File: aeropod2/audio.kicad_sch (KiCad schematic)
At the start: 17 parts, among them J4 AudioJack3_Ground, U5 PCM5102A

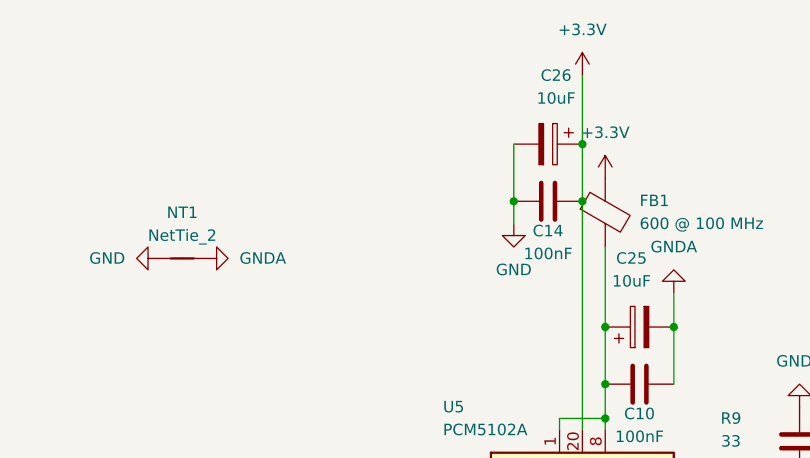
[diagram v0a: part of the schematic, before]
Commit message: Drop button pull-ups and backlight pin, clear ERC, vendor CP2102N footprint
The five button pull-ups are gone. The only line that actually needed one
was B5, because it sat on GPIO35 and GPIO34-39 are input only with no
internal pull-up. B5 now sits on GPIO33, a full GPIO, so the ESP32's own
pull-ups hold all five buttons high and R20-R24 are removed. GPIO35 is
spare.

The display connector goes back to seven pins. There is no backlight
control line, so the module's BL input is tied to 3.3 V and runs at full
brightness. The LEDC setup is removed and display_backlight() is a no-op
so callers do not change.

The five power_pin_not_driven errors are now properly resolved with
PWR_FLAGs on GND, VBUS, VSYS, AVDD and GNDA. To be clear about the VSS
one: that check looks for a power output pin on each rail and finds none
on a rail fed through a diode, ferrite or net tie. It was never a wiring
fault. Before the fixes it named J5 pin 3 CMD, because CMD was wrongly on
the GND net; afterwards it named J5 pin 6 VSS, which is the card's ground
pin and belongs there. The name moved because CMD left the ground net,
which is what the fix was for. Schematic is now 0 errors, 0 warnings.

The microSD wiring was re-verified pin by pin against the SD spec in SPI
mode: DAT2 and DAT1 unused, CS on DAT3/CD, MOSI on CMD, MISO on DAT0,
CLK on pin 5, VDD on pin 4, VSS on GND. All eight correct.

Footprints for every one of the 67 components were checked against what
is on disk. U6 was pointing at a vendor library in a Downloads folder
via a global nickname, so it built here and nowhere else. That library is
now vendored at aeropod2/footprints.pretty with a project fp-lib-table.

Also gitignores KiCad .lck session files.
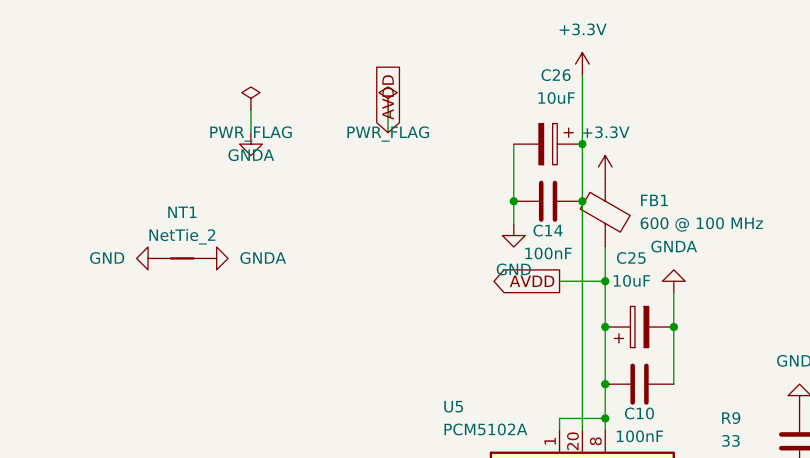
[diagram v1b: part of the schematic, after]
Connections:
- net AVDD: now reaches C10.1, C25.1, FB1.2, U5.1 (CPVDD), U5.8 (AVDD)

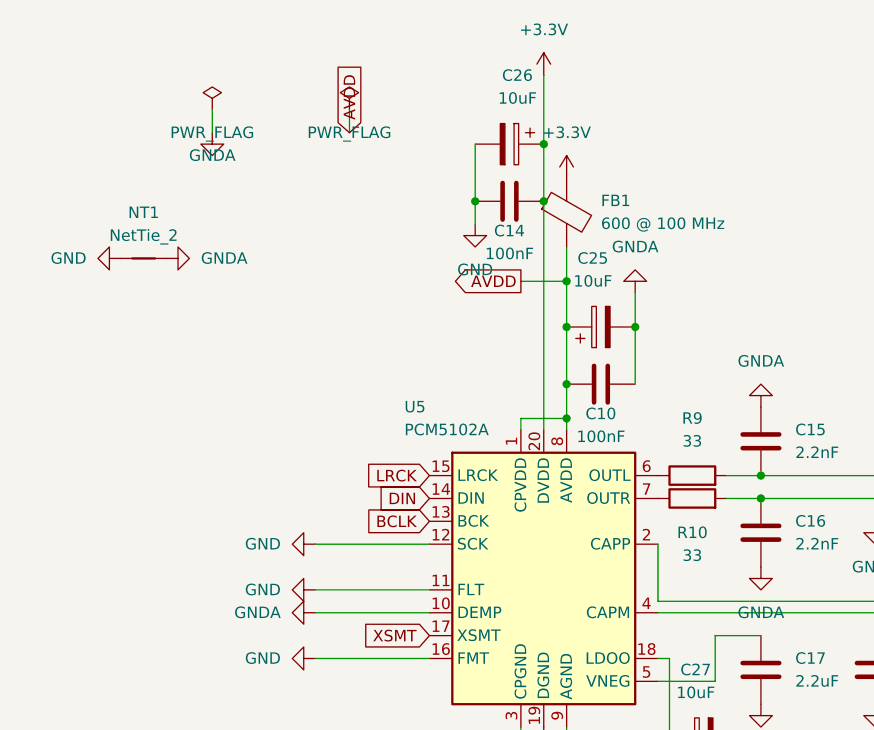
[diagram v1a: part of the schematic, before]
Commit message: Revert schematic, PCB and firmware to the hand-drawn version
Restores aeropod2/*.kicad_sch, aeropod2.kicad_pcb, the firmware pin map
and the BOM to their state at d6429d0, which is byte identical to the
last human-edited revision (2867710). The corrected schematic is still
in history at b35a9fa if any of it is wanted later.

The board file had picked up R18/R19 and the tactile switch footprints
from a schematic update. Nothing hand-made was lost reverting it: track
and via counts were unchanged at 894/147 and the two new parts were
sitting at KiCad's default drop position.

ELECTRICAL_REVIEW.md is rewritten to describe the faults as they stand
in this schematic, and to give the smallest set of layout changes that
makes the board work rather than the full correction.
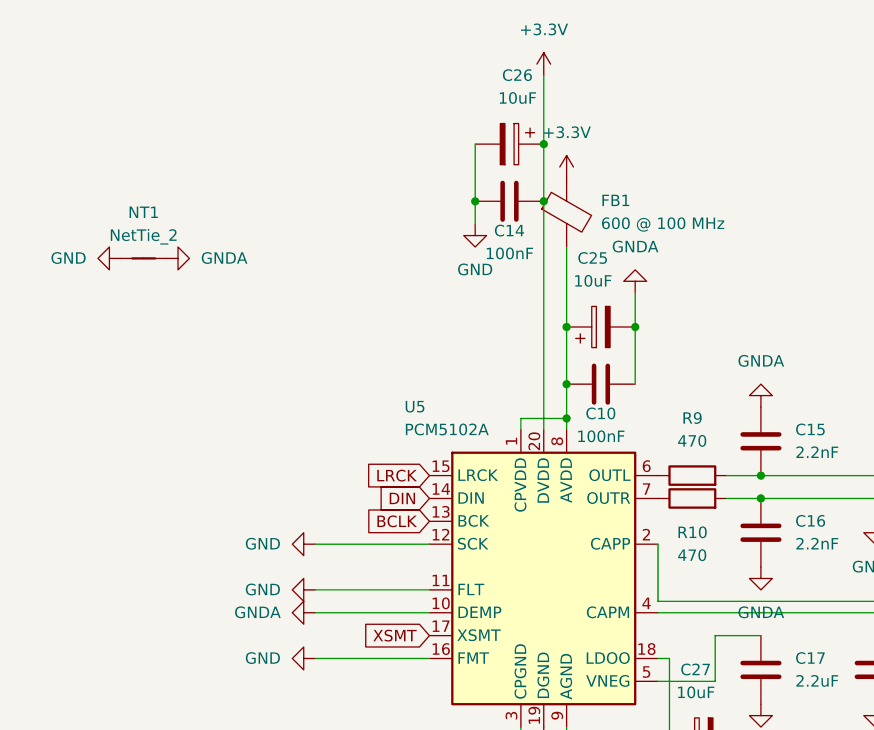
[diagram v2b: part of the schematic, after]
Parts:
- R10, R9: value 33 -> 470
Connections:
- net AVDD: no longer names the net of C10.1, C25.1, FB1.2, U5.1 (CPVDD), U5.8 (AVDD)

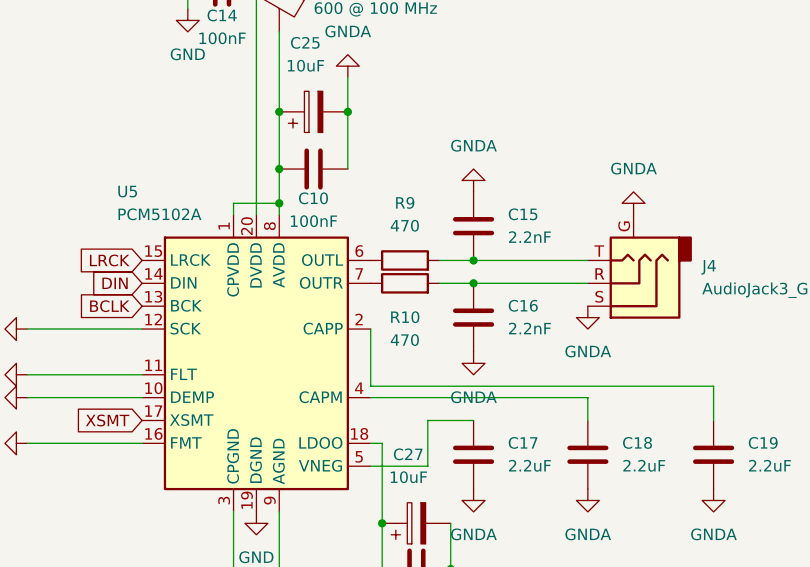
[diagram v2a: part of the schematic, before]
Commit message: Fix schematic faults found in electrical review, add reset/boot buttons
Four faults would have stopped the main board working:

- EN had no pull-up. R4/C5 sat on the unused throw of SW1 while EN was
  left holding only an AC coupled cap, so the module would not have
  booted. R4/C5 now sit on EN, and SW1/SW2 are momentary buttons to
  ground instead of slide switches.
- The microSD was miswired: connections shifted by one pin and CMD tied
  to GND, so no card could ever initialise. The display data line also
  shared a net with the card's DAT0 output. CS now lands on DAT3/CD,
  CMD on IO23 alongside the display, and IO19 is MISO from the card
  alone.
- The boost inductor was never connected to the input rail, so the
  MT3608 had nothing to pump. Rebuilt as VREGIN to L1 to SW plus diode
  anode, with the output caps and feedback divider past the diode.
- The 3.3 V rail had no headroom. R17 is now 100k, putting the boost
  near 5.1 V so the AMS1117 can actually regulate.

Also: backlight control on a new J6 pin 8 driven from IO33, 10k pull-ups
on all five button lines so GPIO35 stops floating, a 100k/100k battery
divider into IO34, both charge LEDs flipped the right way round, 33 ohm
audio series resistors instead of 470, and TP4056 set to about 400 mA.

The CP2102N auto-reset caps are gone. That package brings out RTS but no
DTR, and C30 drove IO0 from CTS, which is an input, so it could not have
worked. Flashing uses the buttons.

Firmware config.h is rewritten against the corrected schematic, and
i2s_output_init now releases the PCM5102A hardware mute on GPIO12, which
nothing was driving.

Schematic passes ERC with no new violations. The PCB has not been
re-laid-out yet, so the main board gerbers are stale; see
ELECTRICAL_REVIEW.md.
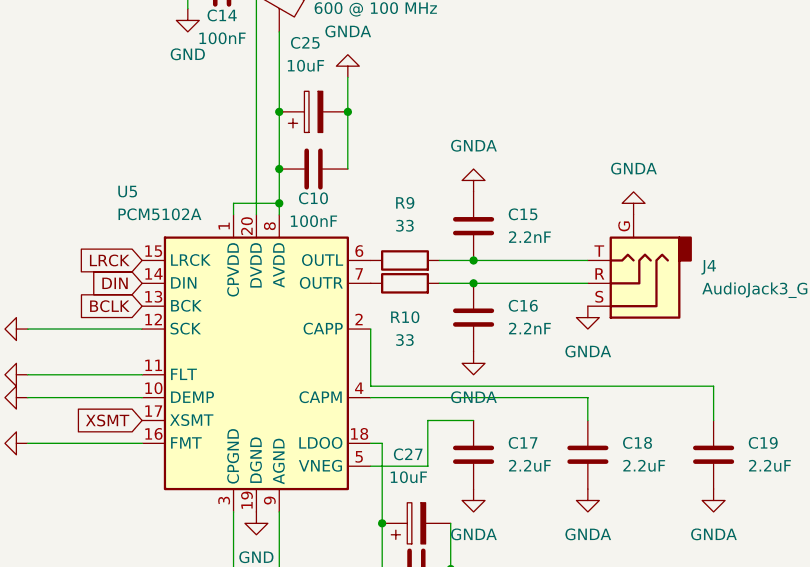
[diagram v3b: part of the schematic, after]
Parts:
- R10, R9: value 470 -> 33
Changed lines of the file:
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@@
 			)
 		)
-		(property "Value" "470"
+		(property "Value" "33"
 			(at 160.02 82.55 90)
 			(show_name no)
@@
 			)
 		)
-		(property "Value" "470"
+		(property "Value" "33"
 			(at 160.02 95.25 90)
 			(show_name no)
